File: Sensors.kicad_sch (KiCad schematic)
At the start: 0 parts

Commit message: sensors?
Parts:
- added C?: C, symbol Device:C
- added J1: Conn_01x03_Socket, Package_SO:HTSSOP-20-1EP_4.4x6.5mm_P0.65mm_EP3.4x6.5mm_ThermalVias, symbol Connector:Conn_01x03_Socket
- added J2: Conn_01x02_Socket, Package_SO:HTSSOP-20-1EP_4.4x6.5mm_P0.65mm_EP3.4x6.5mm_ThermalVias, symbol Connector:Conn_01x02_Socket
- added R?: R, symbol Device:R
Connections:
- new net: C?.2, J2.1 (Pin_1), R?.2
- new net +3V3: J1.1 (Pin_1), R?.1
- new net Ext_Temp: J1.2 (Pin_2)
- new net GND: J1.3 (Pin_3), J2.2 (Pin_2)
- new net Speaker_Out: C?.1
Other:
- note added: "External Temp: DHT22/AM2302"
- note added: "Speaker: CMEJ-4618-42-L177"

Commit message: working on audio dac
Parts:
- added R?: 10k, Resistor_SMD:R_0603_1608Metric, symbol Device:R
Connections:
- net +3V3: now also R?.1
- net Ext_Temp renamed PA_3
- net PA_3: now also R?.2
- net Speaker_Out: no longer names the net of C?.1
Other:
- note added: "Info over serial line"
- moved on the sheet: J1

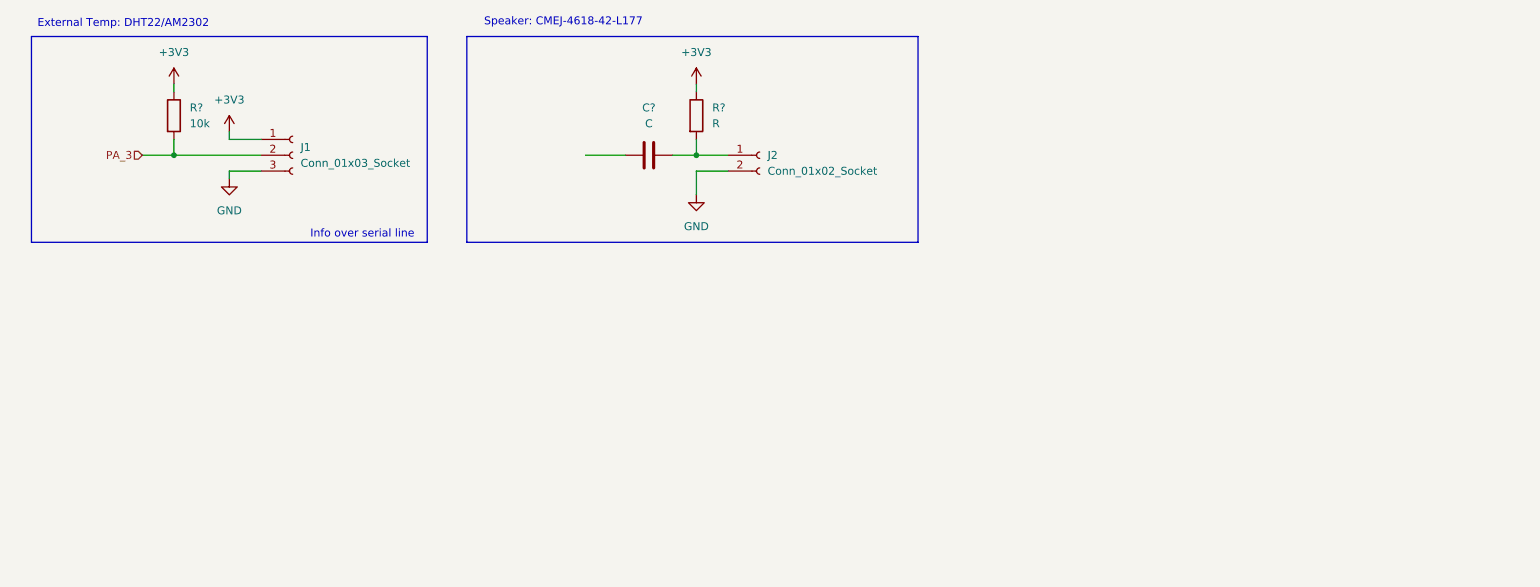
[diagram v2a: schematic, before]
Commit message: added papir, internal temp sensor
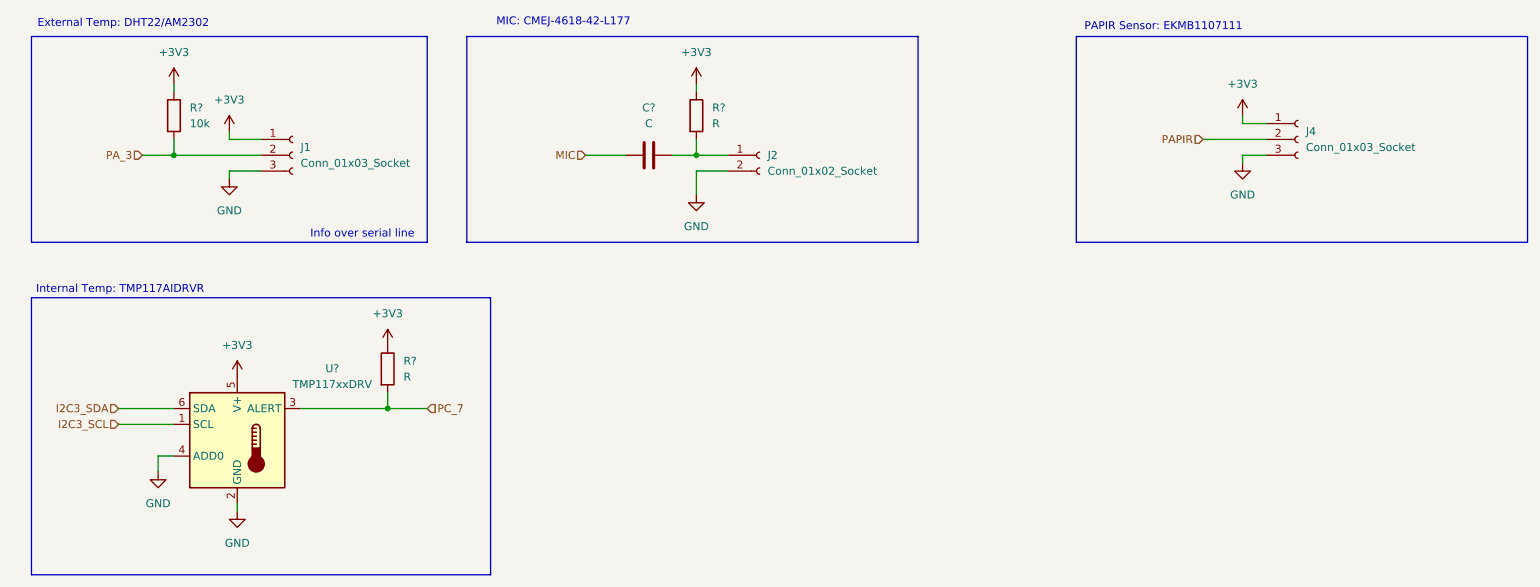
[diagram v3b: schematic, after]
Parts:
- added J4: Conn_01x03_Socket, symbol Connector:Conn_01x03_Socket
- added R?: R, Package_SON:WSON-6-1EP_2x2mm_P0.65mm_EP1x1.6mm, symbol Device:R
- added U?: TMP117xxDRV, Package_SON:WSON-6-1EP_2x2mm_P0.65mm_EP1x1.6mm, symbol Sensor_Temperature:TMP117xxDRV
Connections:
- net +3V3: now also J4.1 (Pin_1), R?.1, U?.5 (V+)
- net GND: now also J4.3 (Pin_3), U?.2 (GND), U?.4 (ADD0)
- net MIC: now reaches C?.1
- new net I2C3_SCL: U?.1 (SCL)
- new net I2C3_SDA: U?.6 (SDA)
- new net PAPIR: J4.2 (Pin_2)
- new net PC_7: R?.2, U?.3 (ALERT)
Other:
- note added: "Internal Temp: TMP117AIDRVR"
- note added: "MIC: CMEJ-4618-42-L177"
- note added: "PAPIR Sensor: EKMB1107111"
- note removed: "Speaker: CMEJ-4618-42-L177"

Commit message: Light sensor
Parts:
- added J5: Conn_01x02_Socket, symbol Connector:Conn_01x02_Socket
- added R?: 10k, Resistor_SMD:R_0603_1608Metric, symbol Device:R
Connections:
- net +3V3: now also J5.1 (Pin_1)
- net GND: now also R?.2
- new net LightSense: J5.2 (Pin_2), R?.1
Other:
- note added: "Light Sensor: TEPT5600"
- moved on the sheet: C?, J2, R?

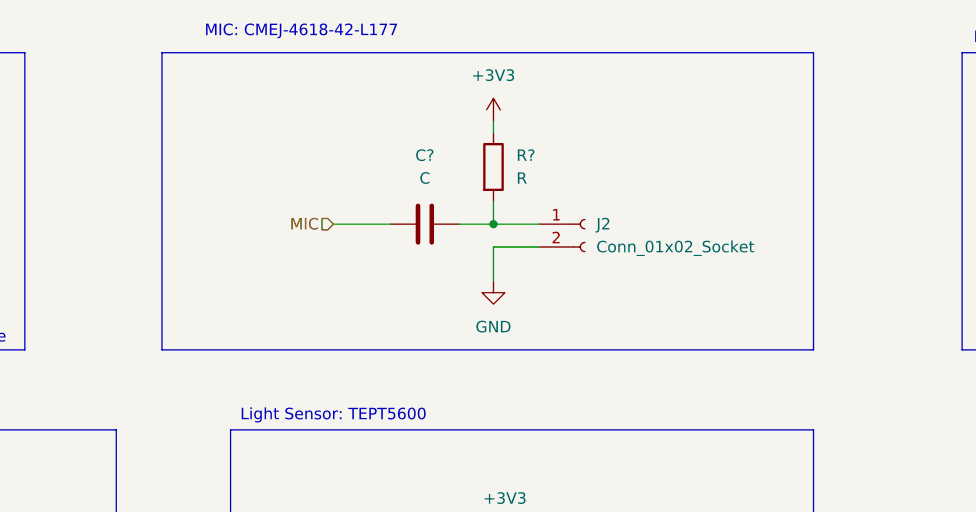
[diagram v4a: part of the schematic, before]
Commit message: fixing audio dac, moving audio to analog section
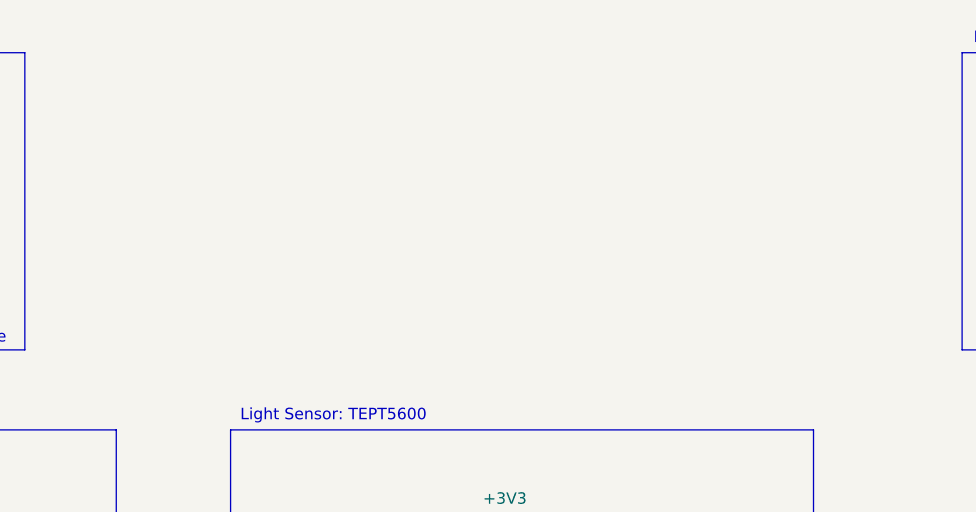
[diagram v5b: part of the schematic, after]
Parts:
- removed C?: C, symbol Device:C
- removed J2: Conn_01x02_Socket, Package_SO:HTSSOP-20-1EP_4.4x6.5mm_P0.65mm_EP3.4x6.5mm_ThermalVias, symbol Connector:Conn_01x02_Socket
- removed R?: R, symbol Device:R
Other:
- note removed: "MIC: CMEJ-4618-42-L177"

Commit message: Minor tweaks
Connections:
- net PA_3 renamed EXT_TEMP
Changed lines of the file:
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@@
 		)
 	)
-	(hierarchical_label "PA_3"
+	(hierarchical_label "EXT_TEMP"
 		(shape input)
 		(at 39.37 40.64 180)

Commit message: Wednesday minor changes
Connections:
- net LightSense renamed ALS_ADC
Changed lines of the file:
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@@
+		)
+	)
+	(text_box "I2C Address: 0x48\n\n"
+		(exclude_from_sim no)
+		(at 71.12 101.4617 0)
+		(size 20.32 3.9483)
+		(margins 0.9525 0.9525 0.9525 0.9525)
+		(stroke
+			(width 0)
+			(type solid)
+		)
+		(fill
+			(type none)
+		)
+		(effects
+			(font
+				(size 1.27 1.27)
+			)
+			(justify left top)
 		)
 	)
@@
 			(width 0)
 			(type default)
+		)
+	)
+	(hierarchical_label "ALS_ADC"
+		(shape input)
+		(at 129.54 81.28 180)
+		(effects
+			(font
+				(size 1.27 1.27)
+			)
+			(justify right)
 		)
 	)
@@
 		(effects
 			(font
-				(size 1.27 1.27)
-			)
-			(justify right)
-		)
-	)
-	(hierarchical_label "LightSense"
-		(shape input)
-		(at 129.54 81.28 180)
-		(effects
-			(font

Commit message: adding footprints to sensors
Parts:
- J1: footprint Package_SO:HTSSOP-20-1EP_4.4x6.5mm_P0.65mm_EP3.4x6.5mm_ThermalVias -> Connector_PinHeader_2.54mm:PinHeader_1x03_P2.54mm_Vertical
- R70: renamed from R?; value R -> 10k; footprint Package_SON:WSON-6-1EP_2x2mm_P0.65mm_EP1x1.6mm -> Resistor_SMD:R_0603_1608Metric
- gave numbers to parts that had none: 2
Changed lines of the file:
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@@
 		(dnp no)
 		(fields_autoplaced yes)
-		(property "Reference" "R?"
+		(property "Reference" "R71"
 			(at 46.99 33.0199 0)
 			(show_name no)
@@
 			(project "SeniorDesign_PCB"
 				(path "/88e1ced0-9576-4565-ab29-f74bf51ccbda/31f163eb-679a-41ad-bd95-ba79c79ee532"
-					(reference "R?")
+					(reference "R71")
 					(unit 1)
 				)
@@
 		(dnp no)
 		(fields_autoplaced yes)
-		(property "Reference" "R?"
+		(property "Reference" "R72"
 			(at 140.97 87.6299 0)
 			(show_name no)
@@
 			(project "SeniorDesign_PCB"
 				(path "/88e1ced0-9576-4565-ab29-f74bf51ccbda/31f163eb-679a-41ad-bd95-ba79c79ee532"
-					(reference "R?")
+					(reference "R72")
 					(unit 1)
 				)
@@
 			)
 		)
-		(property "Footprint" "Package_SO:HTSSOP-20-1EP_4.4x6.5mm_P0.65mm_EP3.4x6.5mm_ThermalVias"
+		(property "Footprint" "Connector_PinHeader_2.54mm:PinHeader_1x03_P2.54mm_Vertical"
 			(at 63.5 40.64 0)
 			(hide yes)
@@
 		(dnp no)
 		(fields_autoplaced yes)
-		(property "Reference" "R?"
+		(property "Reference" "R70"
 			(at 81.28 73.6599 0)
 			(show_name no)
@@
 			)
 		)
-		(property "Value" "R"
+		(property "Value" "10k"
 			(at 81.28 76.1999 0)
 			(show_name no)
@@
 			)
 		)
-		(property "Footprint" "Package_SON:WSON-6-1EP_2x2mm_P0.65mm_EP1x1.6mm"
+		(property "Footprint" "Resistor_SMD:R_0603_1608Metric"
 			(at 76.962 74.93 90)
 			(hide yes)
@@
 			(project "SeniorDesign_PCB"
 				(path "/88e1ced0-9576-4565-ab29-f74bf51ccbda/31f163eb-679a-41ad-bd95-ba79c79ee532"
-					(reference "R?")
-					(unit 1)
-				)
+					(reference "R70")
+					(unit 1)
+				)
